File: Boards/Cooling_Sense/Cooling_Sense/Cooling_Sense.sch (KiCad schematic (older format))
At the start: 46 parts, among them J1 CONN_02X03, J2 MM_F_RA_20, U1 MCP2561-E_SN, U101 TPS560430YF, U2 ATMEGA16M1, Y1 Crystal_SMD

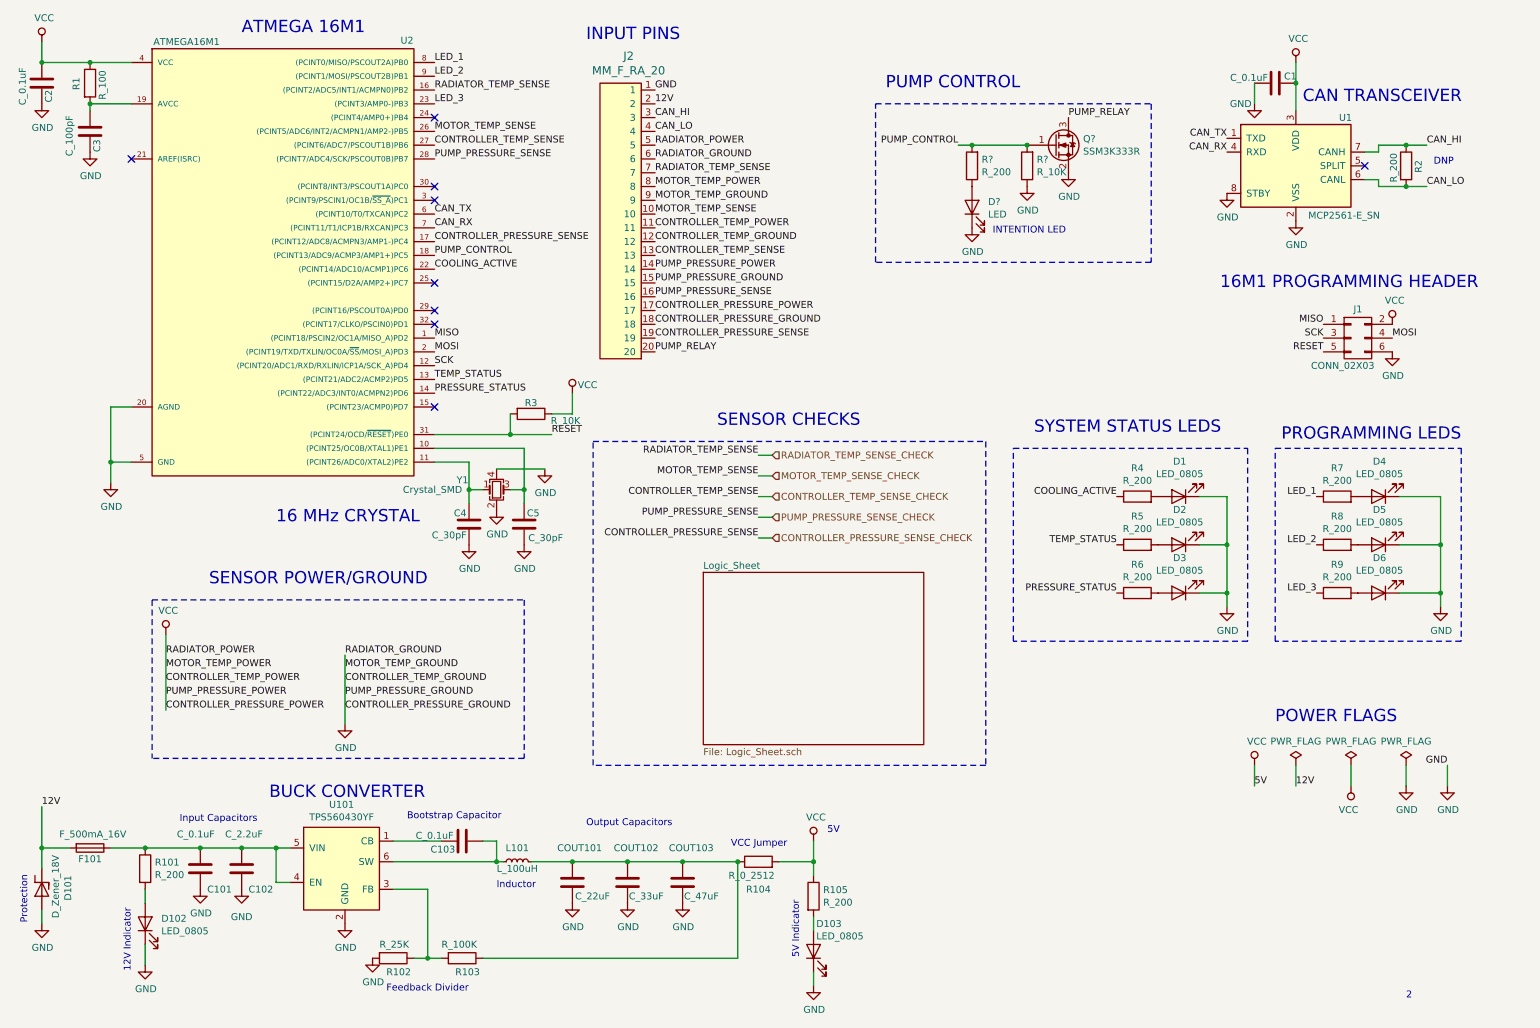
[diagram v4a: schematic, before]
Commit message: updated schematic with new analog circuitry, waiting for ok from manu to proceed
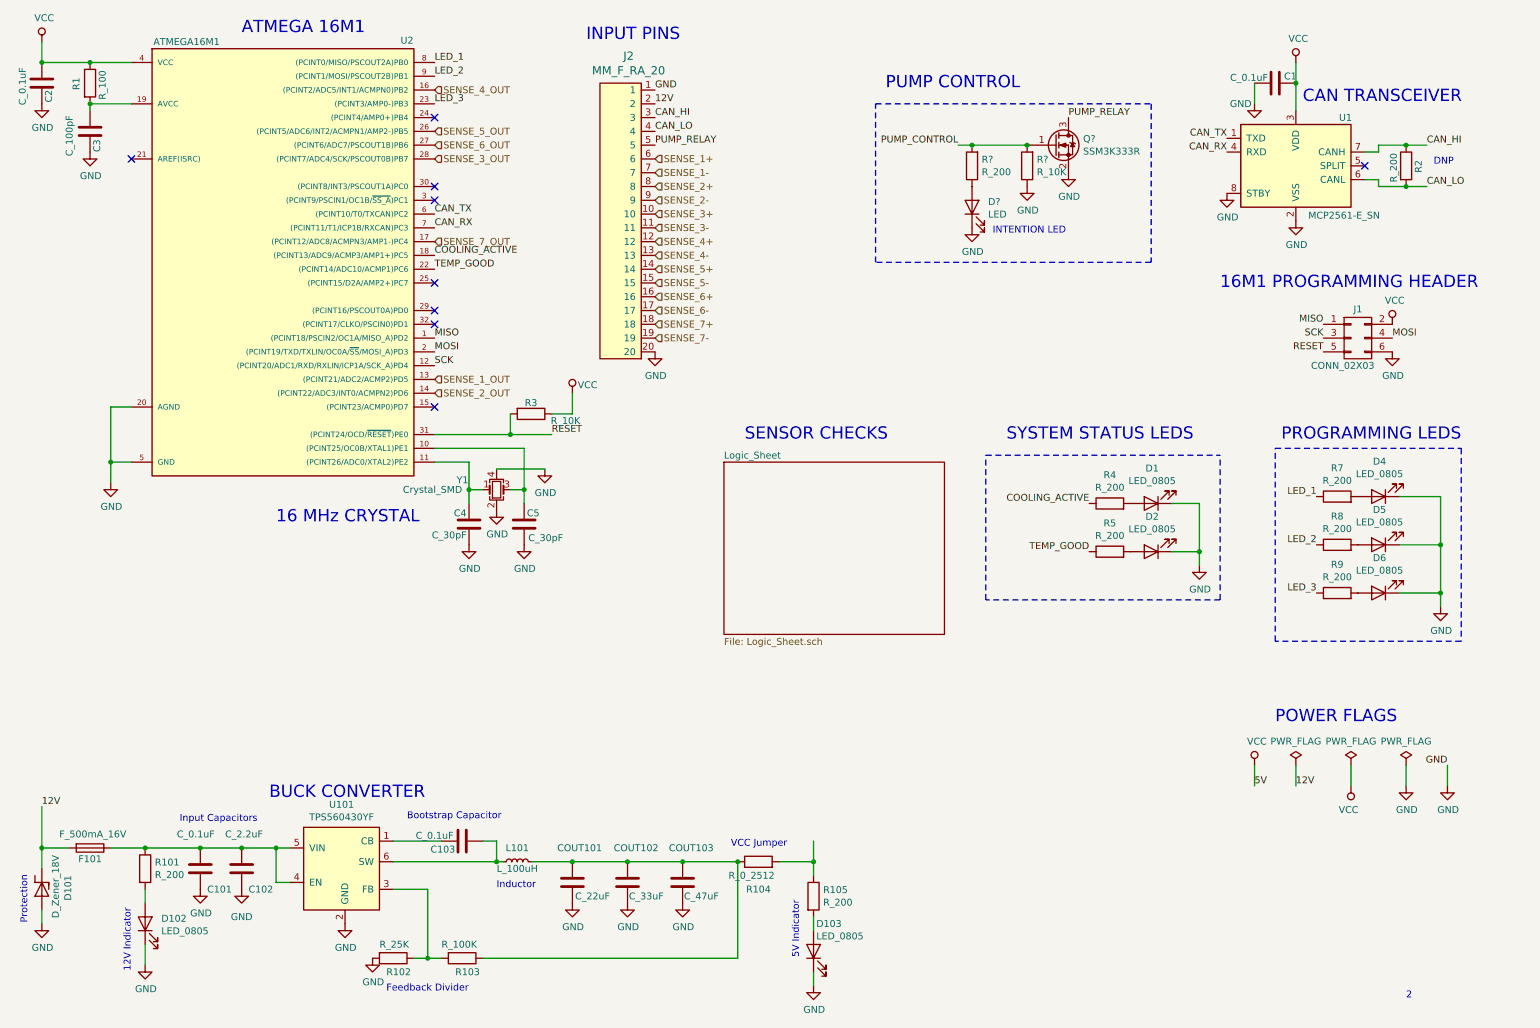
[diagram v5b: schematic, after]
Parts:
- removed D3: LED_0805, footprints:LED_0805_OEM, symbol formula:LED_0805
- removed R6: R_200, footprints:R_0805_OEM, symbol formula:R_200
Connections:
- net COOLING_ACTIVE: now also U2.18 ((PCINT13/ADC9/ACMP3/AMP1+)PC5); no longer U2.22 ((PCINT14/ADC10/ACMP1)PC6)
- net GND: now also J2.20; no longer J2.12, J2.15, J2.18, J2.6, J2.9
- net PUMP_CONTROL: no longer U2.18 ((PCINT13/ADC9/ACMP3/AMP1+)PC5)
- net PUMP_RELAY: now also J2.5; no longer J2.20
- net VCC: no longer J2.11, J2.14, J2.17, J2.5, J2.8, R104.2, R105.1
- net CONTROLLER_PRESSURE_SENSE_CHECK renamed SENSE_7-
- net SENSE_7-: no longer U2.17 ((PCINT12/ADC8/ACMPN3/AMP1-)PC4)
- net CONTROLLER_TEMP_SENSE_CHECK renamed SENSE_4-
- net SENSE_4-: no longer U2.27 ((PCINT6/ADC7/PSCOUT1B)PB6)
- net MOTOR_TEMP_SENSE_CHECK renamed SENSE_3+
- net SENSE_3+: no longer U2.26 ((PCINT5/ADC6/INT2/ACMPN1/AMP2-)PB5)
- net PRESSURE_STATUS renamed SENSE_2_OUT
- net PUMP_PRESSURE_SENSE_CHECK renamed SENSE_3_OUT
- net SENSE_3_OUT: no longer J2.16
- net RADIATOR_TEMP_SENSE_CHECK renamed SENSE_1-
- net SENSE_1-: no longer U2.16 ((PCINT2/ADC5/INT1/ACMPN0)PB2)
- net TEMP_STATUS renamed SENSE_1_OUT
- net SENSE_1_OUT: no longer R5.1
- new net: R104.2, R105.1
- new net SENSE_1+: J2.6
- new net SENSE_2+: J2.8
- new net SENSE_2-: J2.9
- new net SENSE_3-: J2.11
- new net SENSE_4+: J2.12
- new net SENSE_4_OUT: U2.16 ((PCINT2/ADC5/INT1/ACMPN0)PB2)
- new net SENSE_5+: J2.14
- new net SENSE_5-: J2.15
- new net SENSE_5_OUT: U2.26 ((PCINT5/ADC6/INT2/ACMPN1/AMP2-)PB5)
- new net SENSE_6+: J2.16
- new net SENSE_6-: J2.17
- new net SENSE_6_OUT: U2.27 ((PCINT6/ADC7/PSCOUT1B)PB6)
- new net SENSE_7+: J2.18
- new net SENSE_7_OUT: U2.17 ((PCINT12/ADC8/ACMPN3/AMP1-)PC4)
- new net TEMP_GOOD: R5.1, U2.22 ((PCINT14/ADC10/ACMP1)PC6)
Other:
- note removed: "5V"
- note removed: "Output Capacitors\n"
- note removed: "SENSOR POWER/GROUND"
- moved on the sheet: D1, D2, R4, R5

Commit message: minor schematic fixes, began layout
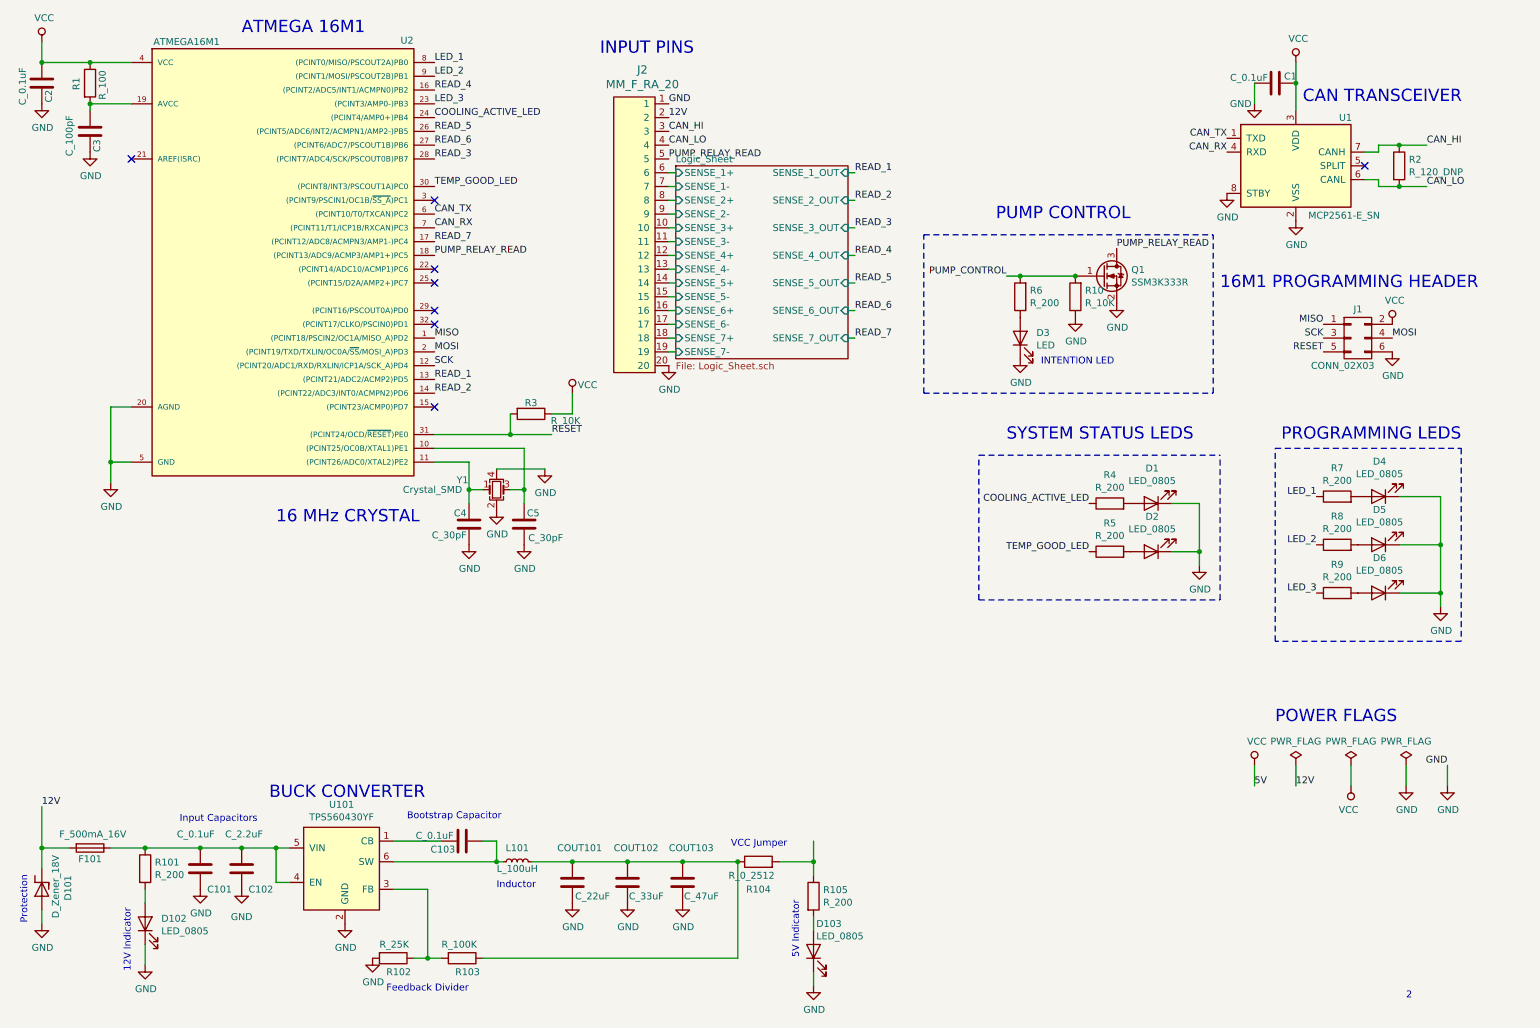
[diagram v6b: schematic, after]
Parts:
- removed R2: R_200, footprints:R_0805_OEM, symbol formula:R_200
- added R2: R_120_DNP, footprints:R_0805_OEM, symbol formula:R_120_DNP
- gave numbers to parts that had none: 4
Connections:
- net PUMP_RELAY is gone; now on net PUMP_RELAY_READ: J2.5, Q1.3 (D)
- net CAN_HI: now also R2.1
- net CAN_LO: now also R2.2
- net COOLING_ACTIVE_LED: now reaches U2.24 ((PCINT4/AMP0+)PB4)
- net COOLING_ACTIVE_LED: now also R4.1
- net TEMP_GOOD_LED: now reaches U2.30 ((PCINT8/INT3/PSCOUT1A)PC0)
- net TEMP_GOOD_LED: now also R5.1
- net COOLING_ACTIVE renamed PUMP_RELAY_READ
- net PUMP_RELAY_READ: no longer R4.1
- net SENSE_1+ renamed Logic_Sheet/SENSE_1+
- net SENSE_1- renamed Logic_Sheet/SENSE_1-
- net SENSE_1_OUT renamed READ_1
- net SENSE_2+ renamed Logic_Sheet/SENSE_2+
- net SENSE_2- renamed Logic_Sheet/SENSE_2-
- net SENSE_2_OUT renamed READ_2
- net SENSE_3+ renamed Logic_Sheet/SENSE_3+
- net SENSE_3- renamed Logic_Sheet/SENSE_3-
- net SENSE_3_OUT renamed READ_3
- net SENSE_4+ renamed Logic_Sheet/SENSE_4+
- net SENSE_4- renamed Logic_Sheet/SENSE_4-
- net SENSE_4_OUT renamed READ_4
- net SENSE_5+ renamed Logic_Sheet/SENSE_5+
- net SENSE_5- renamed Logic_Sheet/SENSE_5-
- net SENSE_5_OUT renamed READ_5
- net SENSE_6+ renamed Logic_Sheet/SENSE_6+
- net SENSE_6- renamed Logic_Sheet/SENSE_6-
- net SENSE_6_OUT renamed READ_6
- net SENSE_7+ renamed Logic_Sheet/SENSE_7+
- net SENSE_7- renamed Logic_Sheet/SENSE_7-
- net SENSE_7_OUT renamed READ_7
- net TEMP_GOOD: no longer names the net of U2.22 ((PCINT14/ADC10/ACMP1)PC6)
- net TEMP_GOOD: no longer R5.1
- no-connect marks 9 -> 8
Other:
- note removed: "DNP"
- note removed: "SENSOR CHECKS\n"
- moved on the sheet: D3, J2, Q1, R10, R6

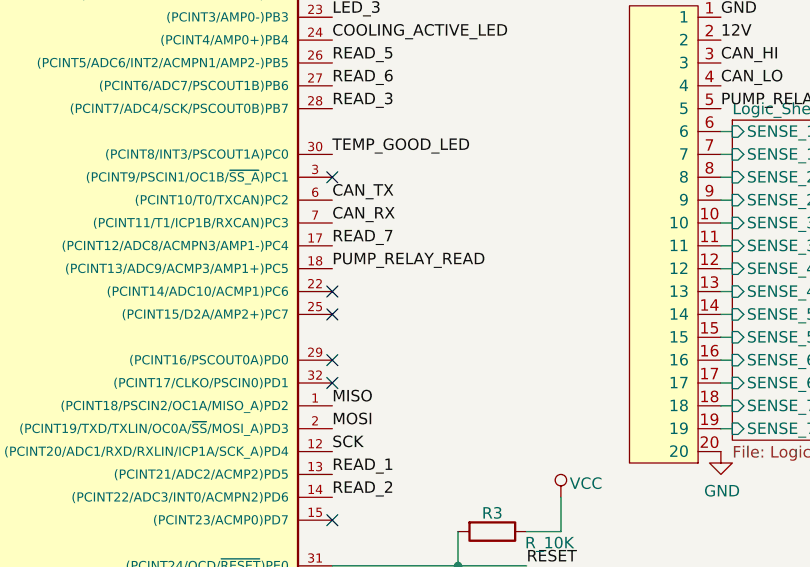
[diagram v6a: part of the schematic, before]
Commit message: began laying traces
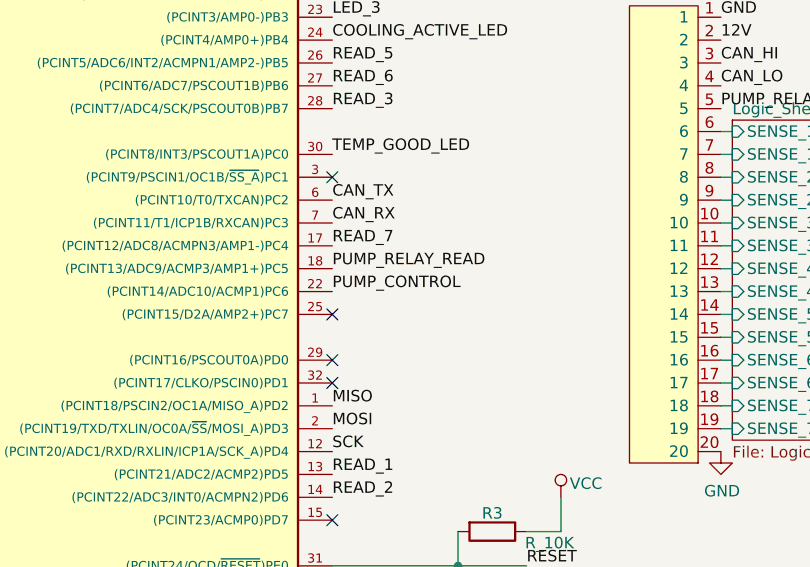
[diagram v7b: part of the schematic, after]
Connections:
- net PUMP_CONTROL: now also U2.22 ((PCINT14/ADC10/ACMP1)PC6)
- no-connect marks 8 -> 7
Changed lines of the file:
@@
 Text Label 5250 1150 0    50   ~ 0
 GND
-NoConn ~ 3550 2350
 NoConn ~ 3550 1850
 NoConn ~ 3550 2450
@@
 Text Label 3550 3250 0    50   ~ 0
 READ_2
+Text Label 3550 2350 0    50   ~ 0
+PUMP_CONTROL
 $EndSCHEMATC

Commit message: done!
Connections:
- net VCC: now also R104.2, R105.1
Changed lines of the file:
@@
 Text Label 3550 2350 0    50   ~ 0
 PUMP_CONTROL
+$Comp
+L power:VCC #PWR?
+U 1 1 5DF48159
+P 6300 6500
+F 0 "#PWR?" H 6300 6350 50  0001 C CNN
+F 1 "VCC" H 6317 6673 50  0000 C CNN
+F 2 "" H 6300 6500 50  0001 C CNN
+F 3 "" H 6300 6500 50  0001 C CNN
+	1    6300 6500
+	1    0    0    -1
+$EndComp
 $EndSCHEMATC
